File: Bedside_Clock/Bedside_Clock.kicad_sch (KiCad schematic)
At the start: 2 parts

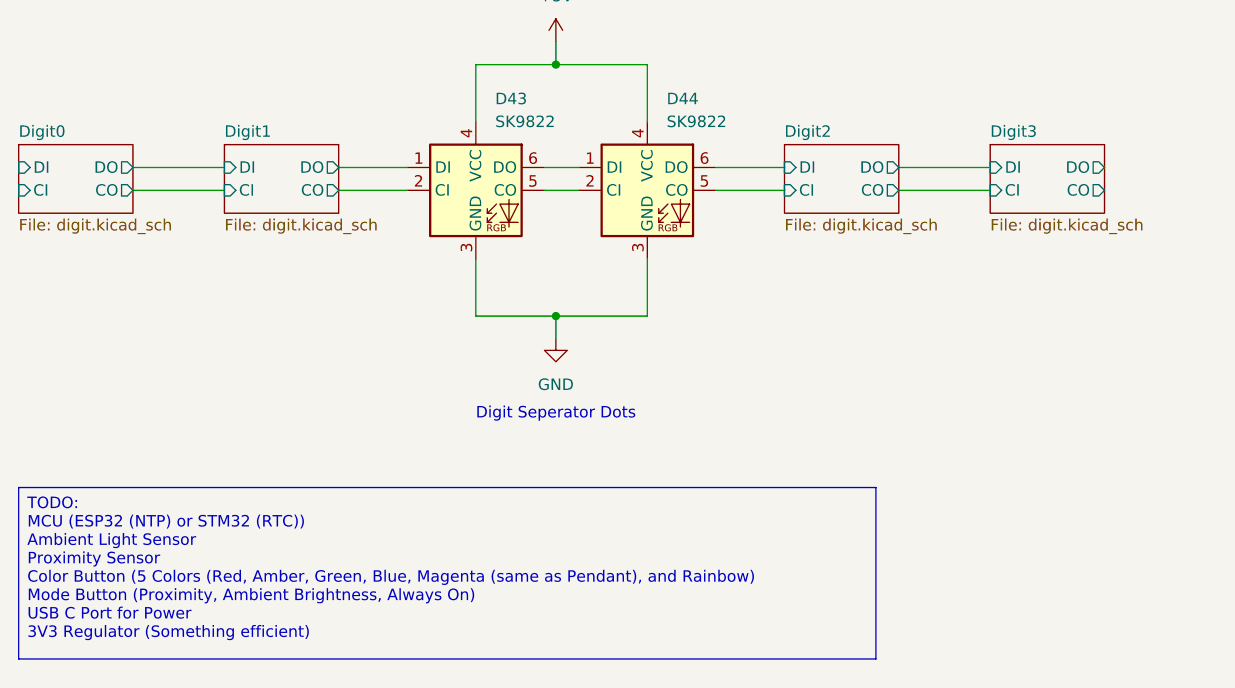
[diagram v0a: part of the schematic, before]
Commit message: [HW] Switch to HD107s (maybe switch to 108s)
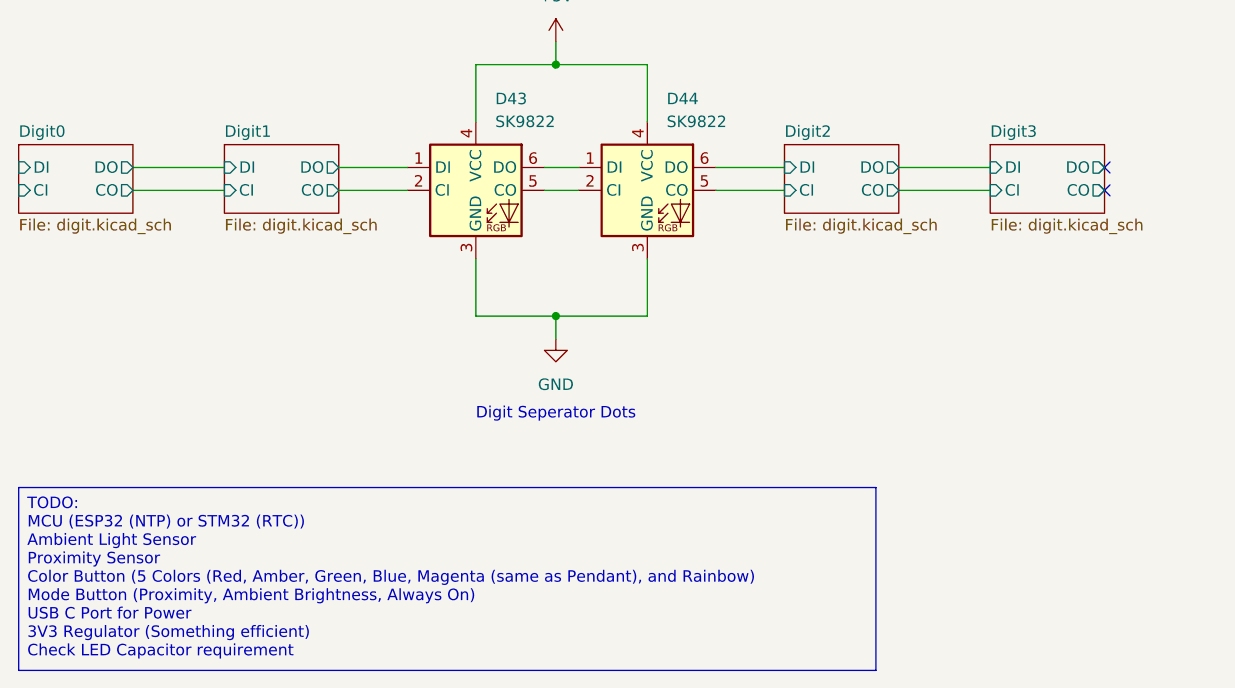
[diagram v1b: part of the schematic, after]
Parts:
- D43, D44: footprint (none) -> LED_SMD:LED_RGB_5050-6; symbol LED:APA102 -> LED:HD107s; Site (none) -> https://www.ledlightinghut.com/hd107s-5050-rgb-led.html
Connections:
- no-connect marks 0 -> 2
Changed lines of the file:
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@@
 		)
 	)
-	(text_box "TODO:\nMCU (ESP32 (NTP) or STM32 (RTC))\nAmbient Light Sensor\nProximity Sensor\nColor Button (5 Colors (Red, Amber, Green, Blue, Magenta (same as Pendant), and Rainbow)\nMode Button (Proximity, Ambient Brightness, Always On)\nUSB C Port for Power\n3V3 Regulator (Something efficient)"
+	(text_box "TODO:\nMCU (ESP32 (NTP) or STM32 (RTC))\nAmbient Light Sensor\nProximity Sensor\nColor Button (5 Colors (Red, Amber, Green, Blue, Magenta (same as Pendant), and Rainbow)\nMode Button (Proximity, Ambient Brightness, Always On)\nUSB C Port for Power\n3V3 Regulator (Something efficient)\nCheck LED Capacitor requirement\n"
 		(exclude_from_sim no)
 		(at 41.91 100.33 0)
-		(size 95.25 19.05)
+		(size 95.25 20.32)
 		(margins 0.9525 0.9525 0.9525 0.9525)
 		(stroke
@@
 		(diameter 0)
 		(color 0 0 0 0)
+	)
+	(no_connect
+		(at 162.56 64.77)
+	)
+	(no_connect
+		(at 162.56 67.31)
 	)
 	(wire
@@
 	)
 	(symbol
-		(lib_id "LED:APA102")
+		(lib_id "LED:HD107s")
 		(at 111.76 67.31 0)
 		(unit 1)
@@
 			)
 		)
-		(property "Footprint" ""
+		(property "Footprint" "LED_SMD:LED_RGB_5050-6"
 			(at 113.03 74.93 0)
 			(effects
@@
 			)
 		)
-		(property "Datasheet" "http://www.led-color.com/upload/201506/APA102%20LED.pdf"
+		(property "Datasheet" "https://www.ledlightinghut.com/files/HD107S.pdf"
 			(at 114.3 76.835 0)
 			(effects
@@
 		)
 		(property "Description" "RGB LED with integrated controller"
+			(at 111.76 67.31 0)
+			(effects
+				(font
+					(size 1.27 1.27)
+				)
+				(hide yes)
+			)
+		)
+		(property "Site" "https://www.ledlightinghut.com/hd107s-5050-rgb-led.html"
 			(at 111.76 67.31 0)
 			(effects
@@
 	)
 	(symbol
-		(lib_id "LED:APA102")
+		(lib_id "LED:HD107s")
 		(at 92.71 67.31 0)
 		(unit 1)
@@
 			)
 		)
-		(property "Footprint" ""
+		(property "Footprint" "LED_SMD:LED_RGB_5050-6"
 			(at 93.98 74.93 0)
 			(effects
@@
 			)
 		)
-		(property "Datasheet" "http://www.led-color.com/upload/201506/APA102%20LED.pdf"
+		(property "Datasheet" "https://www.ledlightinghut.com/files/HD107S.pdf"
 			(at 95.25 76.835 0)
 			(effects
@@
 			(at 92.71 67.31 0)
 			(effects
+				(font
+					(size 1.27 1.27)
+				)
+				(hide yes)
+			)
+		)
+		(property "Site" "https://www.ledlightinghut.com/hd107s-5050-rgb-led.html"
+			(at 92.71 67.31 0)
+			(effects

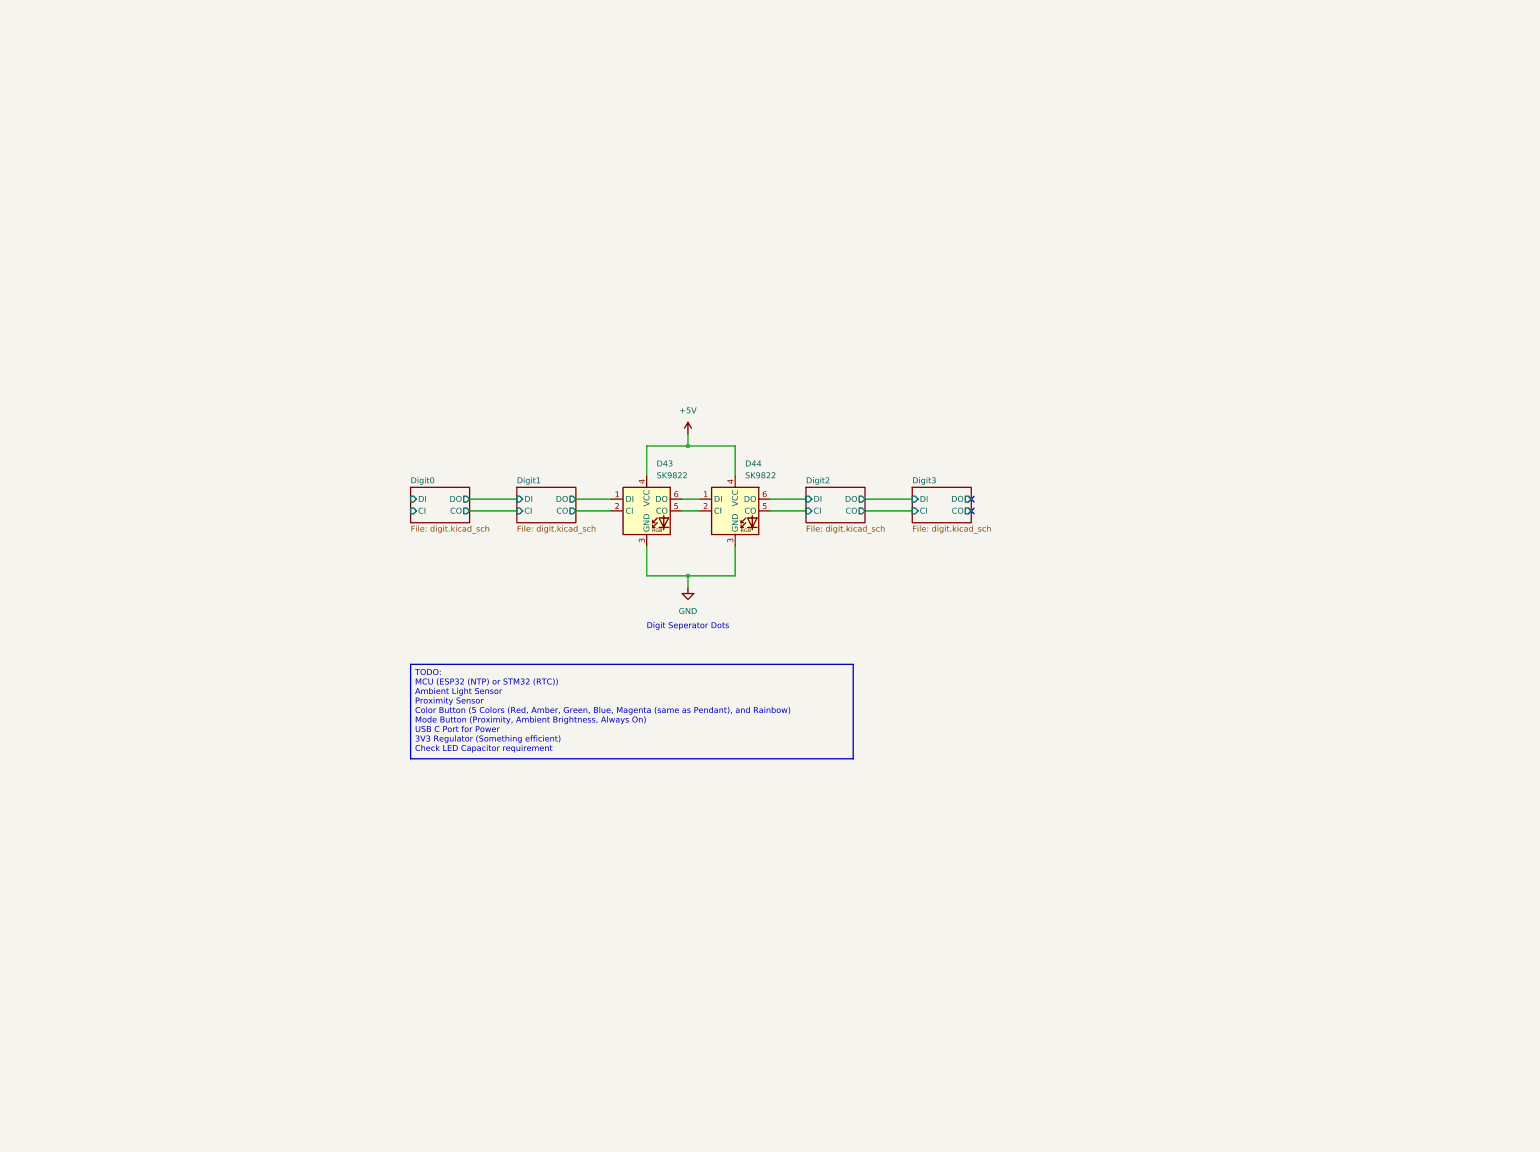
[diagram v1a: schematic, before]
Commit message: [HW] Layout LEDs and first pass add of ESP32 Also add decoupling caps for all LEDs
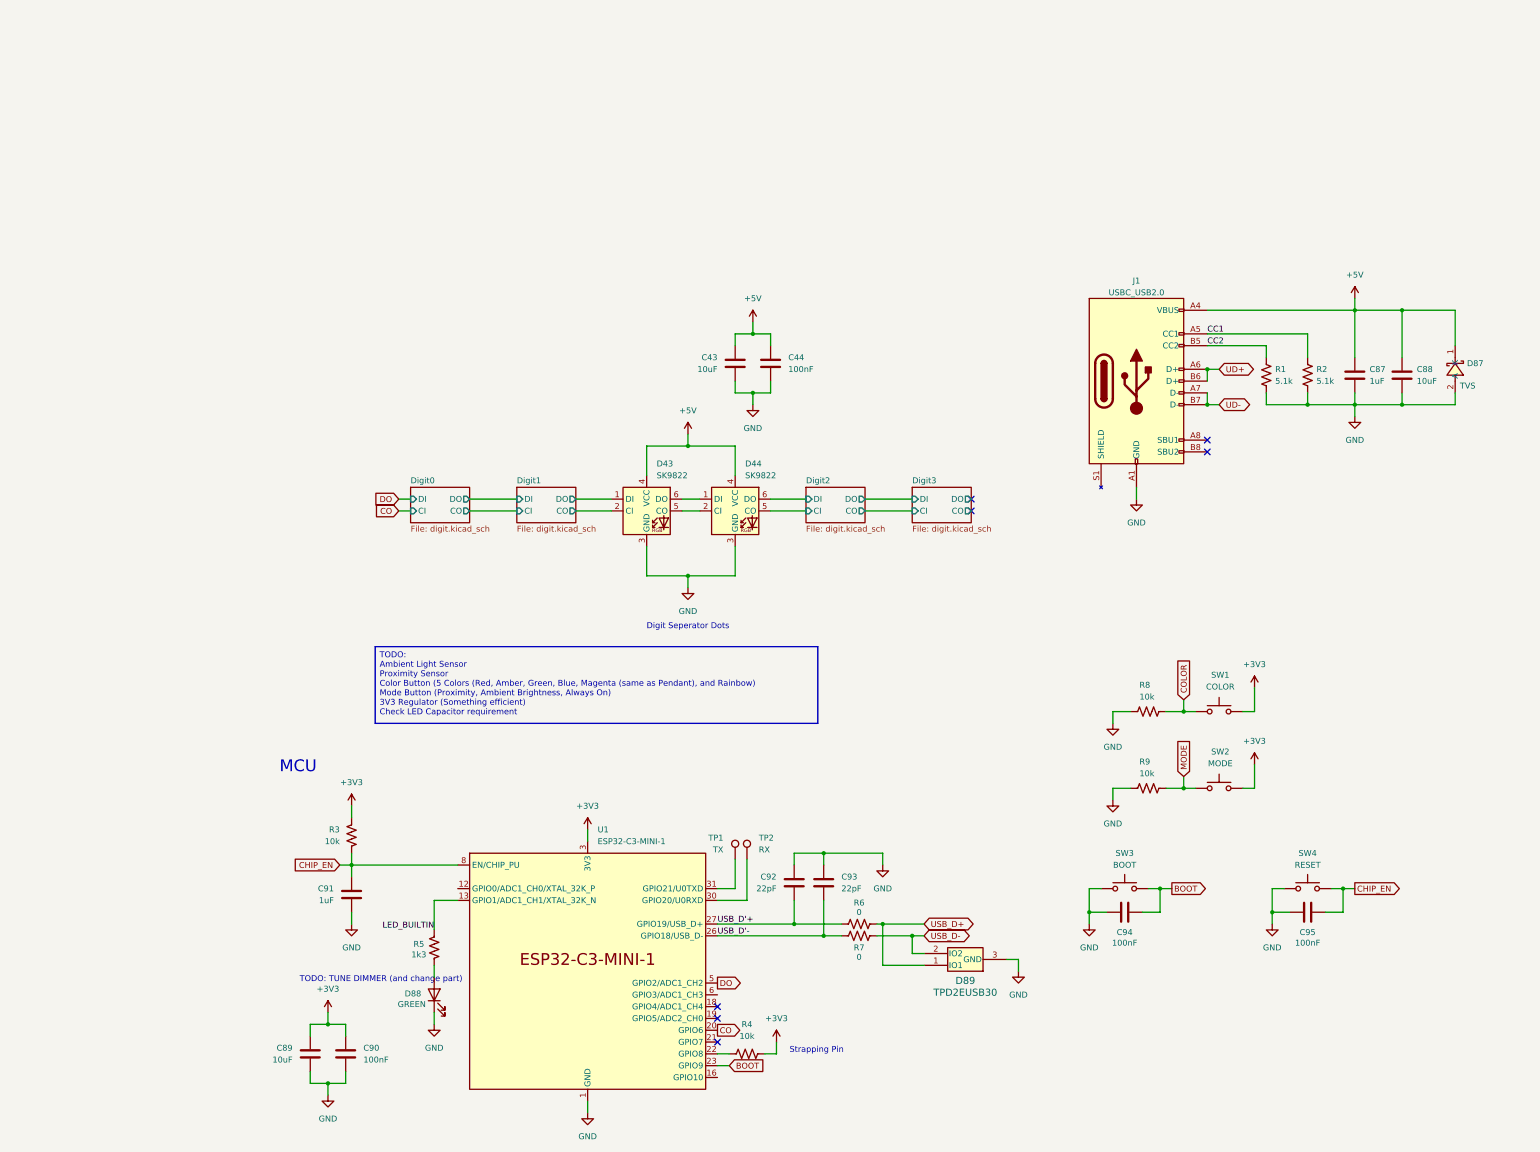
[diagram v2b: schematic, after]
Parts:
- added C43, C88, C89: 10uF, Capacitor_SMD:C_0603_1608Metric, symbol Device:C
- added C44, C90, C94, C95: 100nF, Capacitor_SMD:C_0603_1608Metric, symbol Device:C
- added C87, C91: 1uF, Capacitor_SMD:C_0603_1608Metric, symbol Device:C
- added C92, C93: 22pF, Capacitor_SMD:C_0603_1608Metric, symbol Device:C
- added D87: TVS, EasyEDA2KiCad:X2SON-2_L0.6-W0.3-P0.35_ESD441DPLR, symbol EasyEDA2KiCad:ESD441DPLR
- added D88: GREEN, LED_SMD:LED_0603_1608Metric, symbol Device:LED
- added D89: TPD2EUSB30, EasyEDA2KiCad:SOT-723_L1.2-W0.8-P0.80-LS1.2-BR, symbol TPD2EUSB30DRTR:TPD2EUSB30
- added J1: USBC_USB2.0, Connector_USB:USB_C_Receptacle_GCT_USB4085, symbol Connector:USB_C_Receptacle_USB2.0
- added R1, R2: 5.1k, Resistor_SMD:R_0603_1608Metric, symbol Device:R_US
- added R3, R4: 10k, Resistor_SMD:R_0402_1005Metric, symbol Device:R_US
- added R5: 1k3, Resistor_SMD:R_0402_1005Metric, symbol Device:R_US
- added R6, R7: 0, Resistor_SMD:R_0402_1005Metric, symbol Device:R_US
- added R8, R9: 10k, Resistor_SMD:R_0603_1608Metric, symbol Device:R_US
- added SW1: COLOR, EVQ_P7L01P:SW_EVQ-P7L01P, symbol Switch:SW_Push
- added SW2: MODE, EVQ_P7L01P:SW_EVQ-P7L01P, symbol Switch:SW_Push
- added SW3: BOOT, EasyEDA2KiCad:KEY-SMD_L3.9-W3.0-LS5.0-EH, symbol Switch:SW_Push
- added SW4: RESET, EasyEDA2KiCad:KEY-SMD_L3.9-W3.0-LS5.0-EH, symbol Switch:SW_Push
- added TP1: TX, TestPoint:TestPoint_Pad_D1.0mm, symbol Connector:TestPoint
- added TP2: RX, TestPoint:TestPoint_Pad_D1.0mm, symbol Connector:TestPoint
- added U1: ESP32-C3-MINI-1, EasyEDA2KiCad:WIFIM-SMD_ESP32-C3-MINI-1, symbol MCU_Espressif_Official:ESP32-C3-MINI-1
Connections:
- net +5V: now also C43.1, C44.1, C87.1, C88.1, D87.1 (K), J1.A4 (VBUS), J1.A9 (VBUS), J1.B4 (VBUS), J1.B9 (VBUS)
- net GND: now also C43.2, C44.2, C87.2, C88.2, C89.2, C90.2, C91.2, C92.1, C93.1, C94.2, C95.2, D87.2 (A), D88.1 (K), D89.3 (GND), J1.A1 (GND), J1.A12 (GND), J1.B1 (GND), J1.B12 (GND), R1.1, R2.1, R8.2, R9.2, SW3.1, SW4.1, U1.1 (GND), U1.11 (GND), U1.14 (GND), U1.2 (GND), U1.36 (GND), U1.37 (GND), U1.38 (GND), U1.39 (GND), U1.40 (GND), U1.41 (GND), U1.42 (GND), U1.43 (GND), U1.44 (GND), U1.45 (GND), U1.46 (GND), U1.47 (GND), U1.48 (GND), U1.49 (GND), U1.50 (GND), U1.51 (GND), U1.52 (GND), U1.53 (GND)
- new net: TP2.1, U1.30 (GPIO20/U0RXD)
- new net: D88.2 (A), R5.1
- new net: R4.1, U1.22 (GPIO8)
- new net: TP1.1, U1.31 (GPIO21/U0TXD)
- new net +3V3: C89.1, C90.1, R3.1, R4.2, SW1.1, SW2.1, U1.3 (3V3)
- new net BOOT: C94.1, SW3.2, U1.23 (GPIO9)
- new net CC1: J1.A5 (CC1), R2.2
- new net CC2: J1.B5 (CC2), R1.2
- new net CHIP_EN: C91.1, C95.1, R3.2, SW4.2, U1.8 (EN/CHIP_PU)
- new net CO: U1.20 (GPIO6)
- new net COLOR: R8.1, SW1.2
- new net DO: U1.5 (GPIO2/ADC1_CH2)
- new net LED_BUILTIN: R5.2, U1.13 (GPIO1/ADC1_CH1/XTAL_32K_N)
- new net MODE: R9.1, SW2.2
- new net UD+: J1.A6 (D+), J1.B6 (D+)
- new net UD-: J1.A7 (D-), J1.B7 (D-)
- new net USB_D'+: C92.2, R6.1, U1.27 (GPIO19/USB_D+)
- new net USB_D'-: C93.2, R7.1, U1.26 (GPIO18/USB_D-)
- new net USB_D+: D89.1 (IO1), R6.2
- new net USB_D-: D89.2 (IO2), R7.2
- no-connect marks 2 -> 7
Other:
- note added: "MCU"
- note added: "Strapping Pin"
- note added: "TODO: TUNE DIMMER (and change part)"

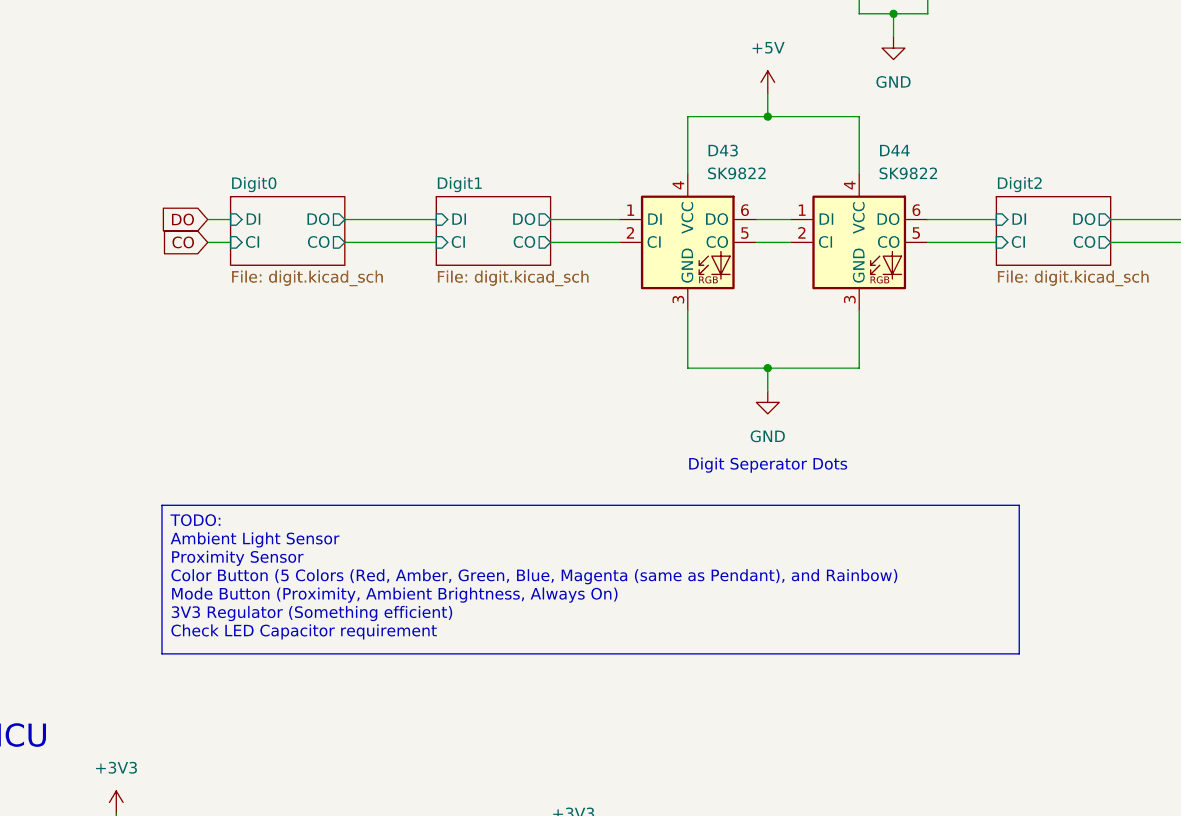
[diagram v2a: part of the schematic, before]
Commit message: [HW] Swap component names from SK9822 to HD107S
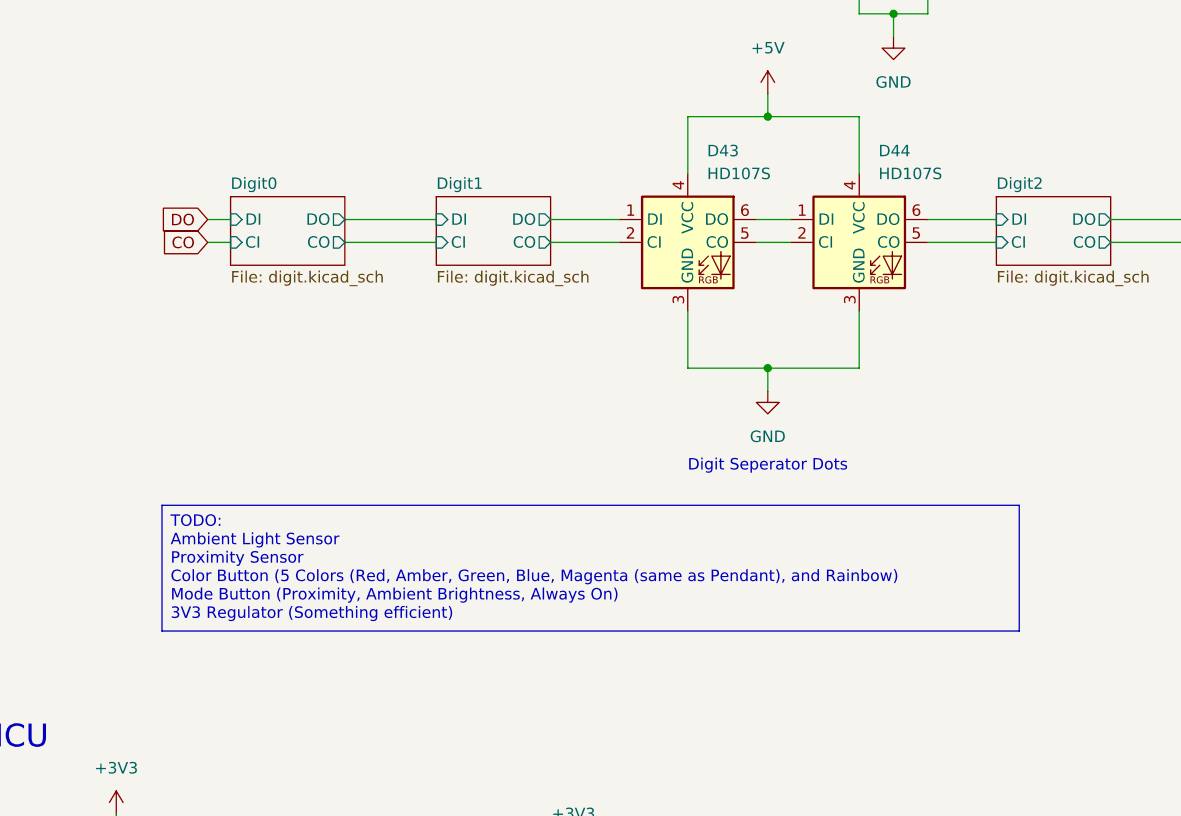
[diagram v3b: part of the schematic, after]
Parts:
- D43, D44: value SK9822 -> HD107S
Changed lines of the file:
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@@
 		)
 	)
-	(text_box "TODO:\nAmbient Light Sensor\nProximity Sensor\nColor Button (5 Colors (Red, Amber, Green, Blue, Magenta (same as Pendant), and Rainbow)\nMode Button (Proximity, Ambient Brightness, Always On)\n3V3 Regulator (Something efficient)\nCheck LED Capacitor requirement\n"
+	(text_box "TODO:\nAmbient Light Sensor\nProximity Sensor\nColor Button (5 Colors (Red, Amber, Green, Blue, Magenta (same as Pendant), and Rainbow)\nMode Button (Proximity, Ambient Brightness, Always On)\n3V3 Regulator (Something efficient)\n"
 		(exclude_from_sim no)
 		(at 34.29 96.52 0)
-		(size 95.25 16.51)
+		(size 95.25 13.97)
 		(margins 0.9525 0.9525 0.9525 0.9525)
 		(stroke
@@
 			)
 		)
-		(property "Value" "SK9822"
+		(property "Value" "HD107S"
 			(at 113.9033 59.69 0)
 			(effects
@@
 			)
 		)
-		(property "Value" "SK9822"
+		(property "Value" "HD107S"
 			(at 94.8533 59.69 0)
 			(effects
